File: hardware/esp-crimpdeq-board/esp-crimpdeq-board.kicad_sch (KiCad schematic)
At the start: 76 parts, among them IC3 ADS1230IPWR, J1 USB4105-GF-A, J2 Conn_01x02_Pin, J3 Conn_01x04_Pin, J4 Conn_01x08_Pin, J5 Conn_01x02, Q1 DMG3415U, SW1 SW_Push, SW2 SW_Push, U1 SHTC3, U2 ICM-42670-P, U3 REF35330QDBVR, U4 SY8088, U6 MCP73831T-2ACI/OT, U7 MAX17262, U8 ESP32-C6-MINI-1/U, Y1 32.768Hz

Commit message: Separated in sheets
-Pending expose lines.
-Change DC/DC
-ADS1235
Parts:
- removed C1, C11, C19, C2: 10nF 10V, Capacitor_SMD:C_0402_1005Metric, symbol Device:C_Small
- removed C10, C23, C25, C8: 1uF 16V, Capacitor_SMD:C_0402_1005Metric, symbol Device:C_Small
- removed C12, C13: DNP, Capacitor_SMD:C_0402_1005Metric, symbol Device:C_Small
- removed C14: 1nF 10V, Capacitor_SMD:C_0402_1005Metric, symbol Device:C_Small
- removed C15, C16: 4.7uF 16V, Capacitor_SMD:C_0603_1608Metric, symbol Device:C_Small
- removed C17: 0.47uF 16V, Capacitor_SMD:C_0603_1608Metric, symbol Device:C_Small
- removed C18: 0.1uF 16V, Capacitor_SMD:C_0603_1608Metric, symbol Device:C_Small
- removed C20, C3, C4, C9: 100nF 10V, Capacitor_SMD:C_0402_1005Metric, symbol Device:C_Small
- removed C22, C24, C29, C30, C31: 0.1uF 10V, Capacitor_SMD:C_0402_1005Metric, symbol Device:C_Small
- removed C28, C5, C7: 10uF 16V, Capacitor_SMD:C_0805_2012Metric, symbol Device:C_Small
- removed C6: 22pF 50V, Capacitor_SMD:C_0603_1608Metric, symbol Device:C_Small
- removed D1: LESD8D3.3CAT5G, Diode_SMD:D_SOD-882, symbol Device:D_TVS
- removed D3: LED, LED_SMD:LED_0603_1608Metric, symbol Device:LED
- removed D4, D6: B5819W, Diode_SMD:D_SOD-123, symbol Device:D_Schottky
- removed D5, D7, D8: LESD5D5.0CT1G, Diode_SMD:D_SOD-523, symbol Device:D_TVS
- removed D9: WS2812B, LED_SMD:LED_WS2812B_PLCC4_5.0x5.0mm_P3.2mm, symbol LED:WS2812B
- removed IC3: ADS1230IPWR, Package_SO:TSSOP-16_4.4x5mm_P0.65mm, symbol PCM_Texas_Instruments:ADS1230IPWR
- removed J1: USB4105-GF-A, PCM_GCT:GCT_USB4105-GF-A, symbol PCM_GCT:USB4105-GF-A
- removed J2: Conn_01x02_Pin, Connector_PinHeader_1.27mm:PinHeader_1x02_P1.27mm_Vertical, symbol Connector:Conn_01x02_Pin
- removed J3: Conn_01x04_Pin, Connector_PinHeader_1.27mm:PinHeader_1x02_P1.27mm_Vertical, symbol Connector:Conn_01x04_Pin
- removed J4: Conn_01x08_Pin, Connector_PinHeader_1.27mm:PinHeader_1x08_P1.27mm_Vertical, symbol Connector:Conn_01x08_Pin
- removed J5: Conn_01x02, symbol Connector_Generic:Conn_01x02
- removed L1: SPH4018H2R2MT (2.2uH 2.2A), Inductor_SMD:L_Bourns-SRN4018, symbol Device:L_Small
- removed Q1: DMG3415U, Package_TO_SOT_SMD:SOT-23, symbol Transistor_FET:DMG2301L
- removed R1, R16, R17, R18, R19, R20, R21, R22, R23, R8, R9: 10kR 1%, Resistor_SMD:R_0402_1005Metric, symbol Device:R_Small_US
- removed R11, R5, R7: 0R 1%, Resistor_SMD:R_0402_1005Metric, symbol Device:R_Small_US
- removed R12: DNP, Resistor_SMD:R_0402_1005Metric, symbol Device:R_Small_US
- removed R14: 1kR 1%, Resistor_SMD:R_0402_1005Metric, symbol Device:R_Small_US
- removed R15, R2: 100kR 1%, Resistor_SMD:R_0402_1005Metric, symbol Device:R_Small_US
- removed R3: 22k1R 1%, Resistor_SMD:R_0402_1005Metric, symbol Device:R_Small_US
- removed R4, R6: 5k1R 1%, Resistor_SMD:R_0402_1005Metric, symbol Device:R_Small_US
- removed S1: 450404015514, PCM_Wurth_Elektronik:450404015514, symbol PCM_Wurth_Elektronik:450404015514
- removed SW1, SW2: SW_Push, Button_Switch_SMD:SW_SPST_PTS810, symbol Switch:SW_Push
- removed U1: SHTC3, PCM_Sensirion:SON100P200X200X80-5N, symbol PCM_Sensirion:SHTC3
- removed U2: ICM-42670-P, PCM_TDK_InvenSense:IC_ICM-42670-P, symbol PCM_TDK_InvenSense:ICM-42670-P
- removed U3: REF35330QDBVR, Package_TO_SOT_SMD:SOT-23-6, symbol Reference_Voltage:REF35330QDBVR
- removed U4: SY8088, Package_TO_SOT_SMD:SOT-23-5, symbol PCM_Silergy:SY8088
- removed U6: MCP73831T-2ACI/OT, Package_TO_SOT_SMD:SOT-23-5, symbol Battery_Management:MCP73831-2-OT
- removed U7: MAX17262, Package_BGA:WLP-9_1.468x1.448mm_Layout3x3_P0.4mm, symbol PCM_Maxim:MAX17262
- removed U8: ESP32-C6-MINI-1/U, PCM_Espressif:ESP32-C6-MINI-1, symbol PCM_Espressif:ESP32-C6-MINI-1/U
- removed Y1: 32.768Hz, Crystal:Crystal_SMD_3215-2Pin_3.2x1.5mm, symbol Device:Crystal
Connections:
- no-connect marks 3 -> 0
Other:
- added sheet ADC (adc.kicad_sch)
- added sheet Actuators (actuators.kicad_sch)
- added sheet Connectors (connectors.kicad_sch)
- added sheet I2C Sensors (i2c_sensors.kicad_sch)
- added sheet Micro controller (ucontroller.kicad_sch)
- added sheet Power management (power_management.kicad_sch)
- note removed: "ADC1 (ADS1230)"
- note removed: "Address: 0x14 (1101000b)"
- note removed: "Address: 0x68 (1101000b)"
- note removed: "Address: 0x70 (1110000b)"
- note removed: "Buttons (Reset & Boot)"
- note removed: "DC/DC Buck Converter 3V3 Rails"
- note removed: "Do not populate!"
- note removed: "ESP32-C6-MINI-1 Module"
- note removed: "External NTC for battery temeprature monitor"
- note removed: "External connectors"
- note removed: "High speed option"
- note removed: "I2C Bus Sensors"
- note removed: "Interrupts can be with pull-up internaly."
- note removed: "LED RGB"
- note removed: "LF Crystal 32.768Hz Do Not Populate"
- note removed: "Li-Ion Charge Management Controller"
- note removed: "REF. VOLTAGE"
- note removed: "Red LED 060 Charging"
- note removed: "SIMPLE ON/OFF"
- note removed: "TODO: I2C vs SPI2 pins check"
- note removed: "USB & Battery Switch"
- note removed: "USB Type-C Connector"

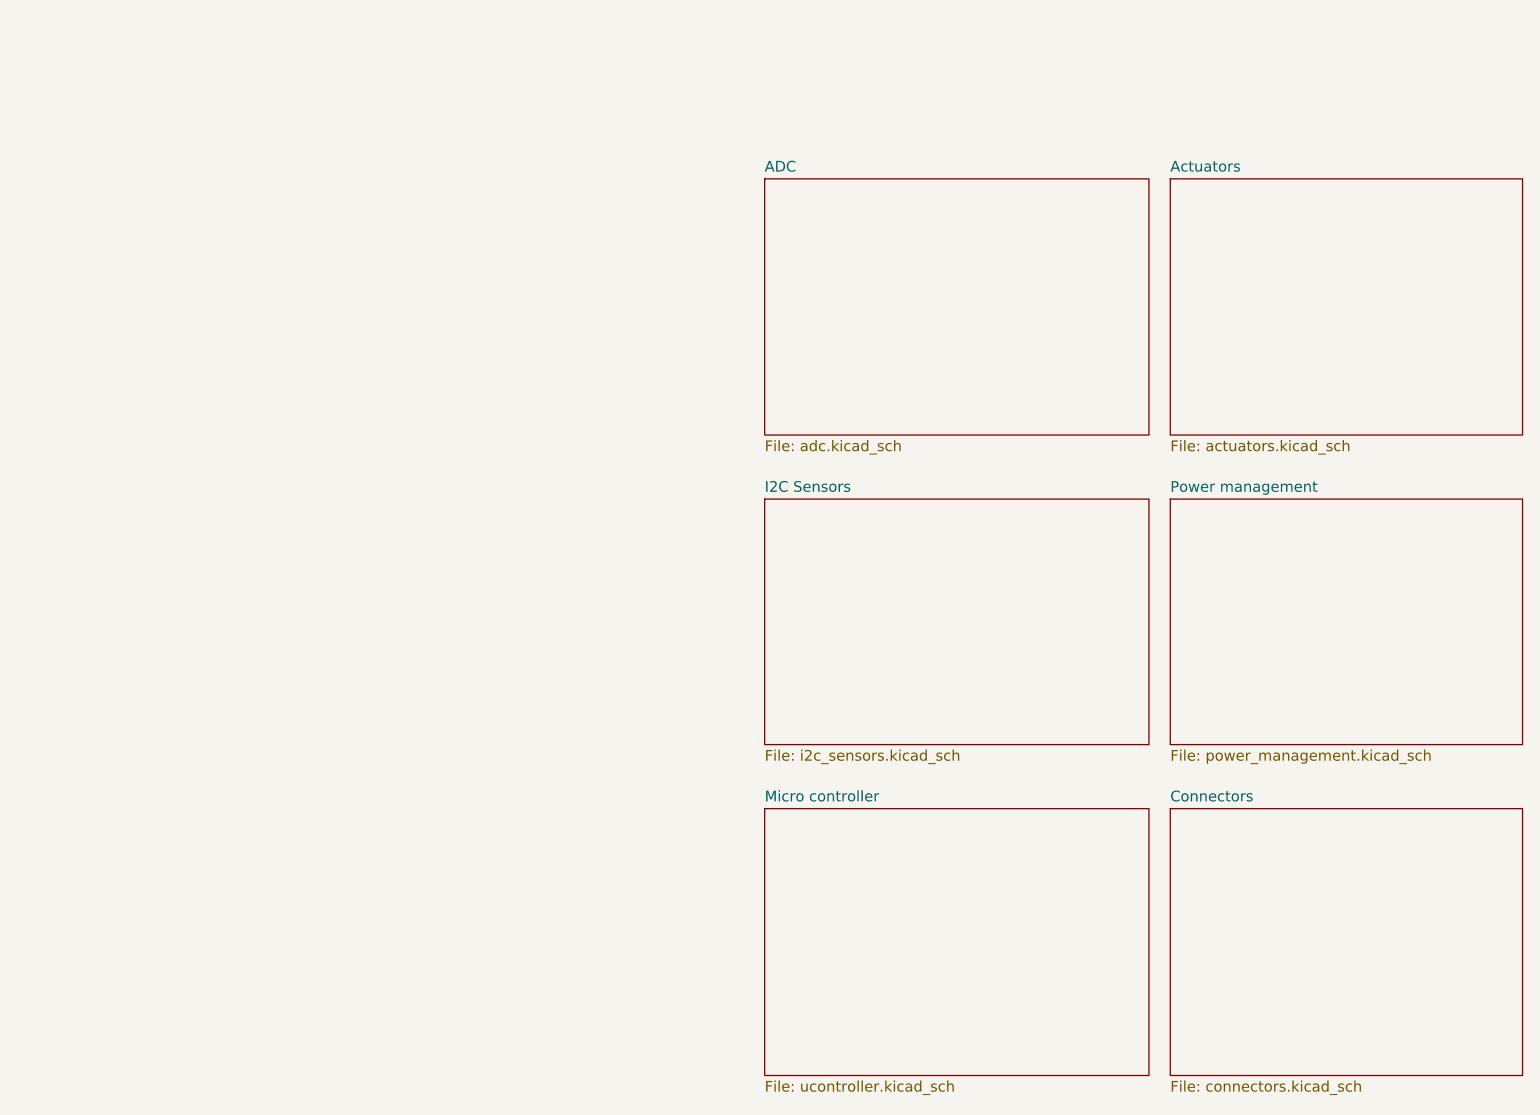
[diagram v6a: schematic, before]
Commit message: Ordering sdchematic in different sheets
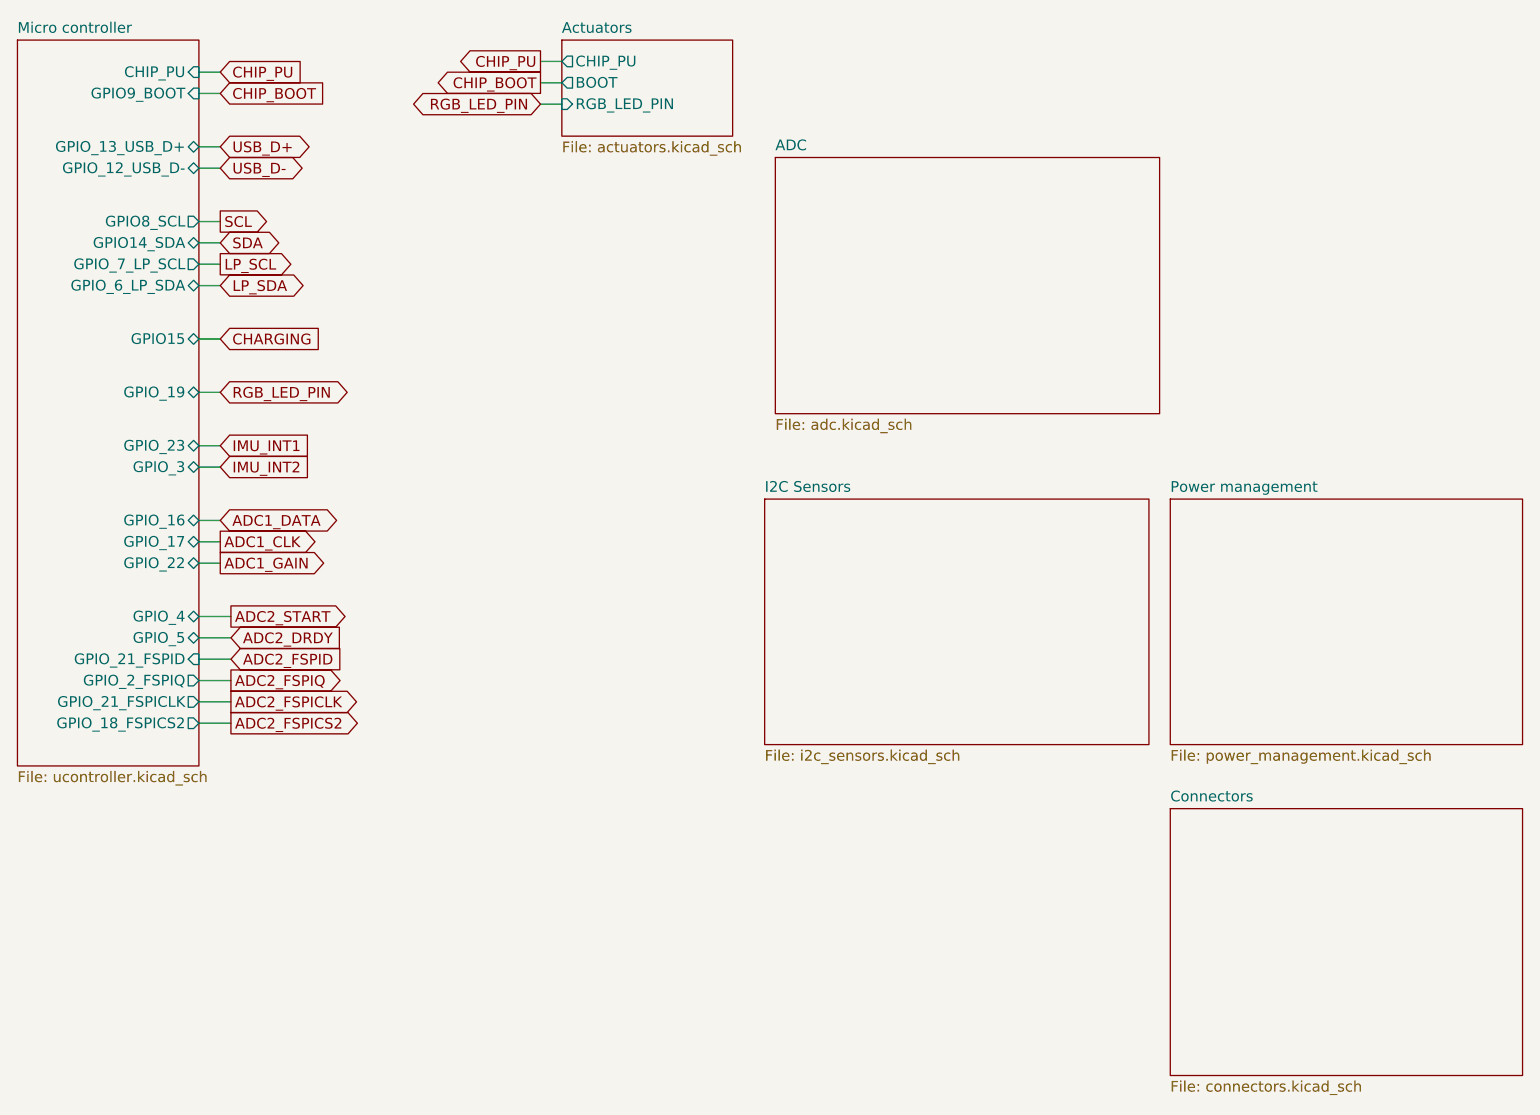
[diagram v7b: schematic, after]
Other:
- sheet Actuators ports: added BOOT, CHIP_PU, RGB_LED_PIN; removed none
- sheet Micro controller ports: added CHIP_PU, GPIO14_SDA, GPIO15, GPIO8_SCL, GPIO9_BOOT, GPIO_12_USB_D-, GPIO_13_USB_D+, GPIO_16, GPIO_17, GPIO_18_FSPICS2, GPIO_19, GPIO_21_FSPICLK, GPIO_21_FSPID, GPIO_22, GPIO_23, GPIO_2_FSPIQ, GPIO_3, GPIO_4, GPIO_5, GPIO_6_LP_SDA, GPIO_7_LP_SCL; removed none
- title: ESP32-C3-Crimpdeq-Board -> ESP32-C6-Crimpdeq-Board

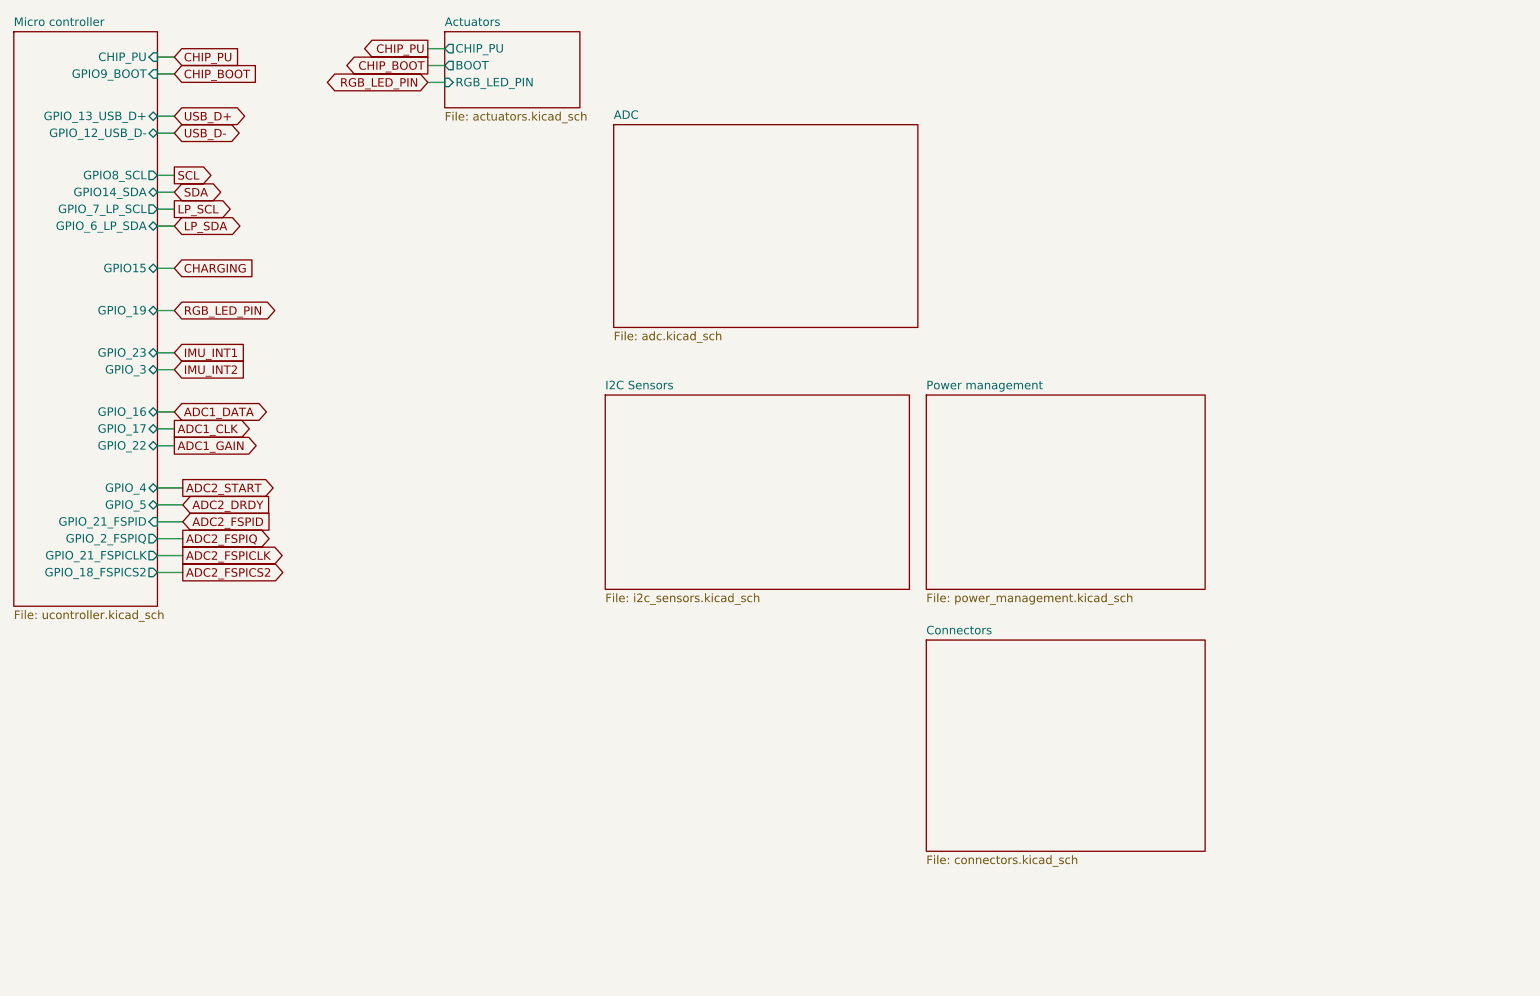
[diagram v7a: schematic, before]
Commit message: Cleaned schematic
- Pending connectors
- Pending BOM and footprints review
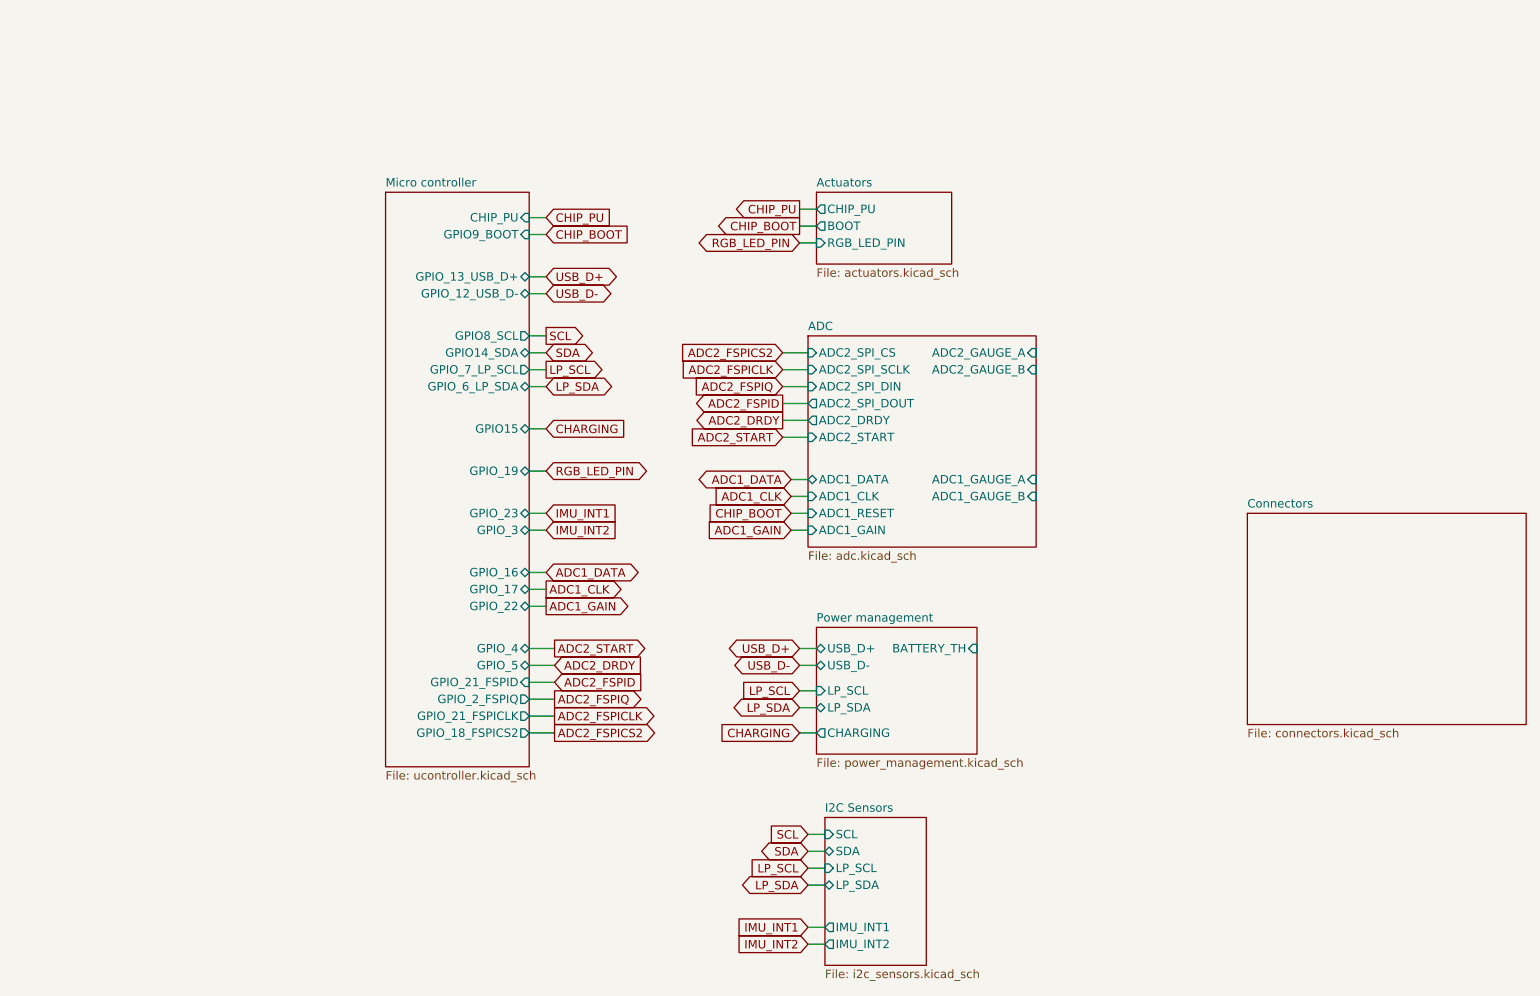
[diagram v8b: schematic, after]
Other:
- sheet ADC ports: added ADC1_CLK, ADC1_DATA, ADC1_GAIN, ADC1_GAUGE_A, ADC1_GAUGE_B, ADC1_RESET, ADC2_DRDY, ADC2_GAUGE_A, ADC2_GAUGE_B, ADC2_SPI_CS, ADC2_SPI_DIN, ADC2_SPI_DOUT, ADC2_SPI_SCLK, ADC2_START; removed none
- sheet I2C Sensors ports: added IMU_INT1, IMU_INT2, LP_SCL, LP_SDA, SCL, SDA; removed none
- sheet Power management ports: added BATTERY_TH, CHARGING, LP_SCL, LP_SDA, USB_D+, USB_D-; removed none
